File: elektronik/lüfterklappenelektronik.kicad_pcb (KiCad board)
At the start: 4 copper layers, 80 x 87.6 mm, 115 parts, among them J101 Conn_01x05_Male, J102 Ckmtw_2510S-2P, J103 Conn_LAN_ENC28J60, J104 USB_B_Micro, J106 WJ2EDGVC-5.08-2P, J107 WJ2EDGVC-5.08-2P, J108 WJ2EDGVC-5.08-2P, P101 PWR_BUS_CONN1, P103 PressureSensor3, P104 PressureSensor1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

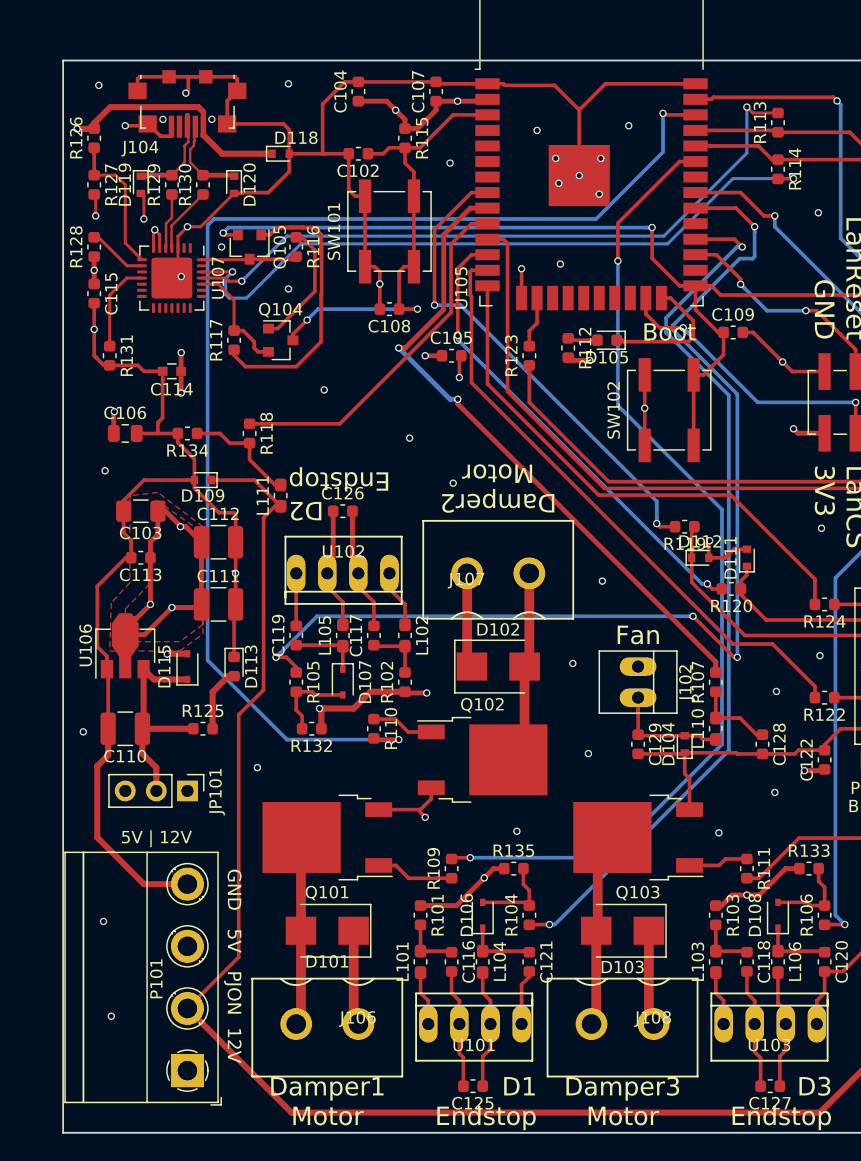
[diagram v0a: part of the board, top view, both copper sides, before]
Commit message: pcbnew: change footprint to vertical and fix fillzones and traces
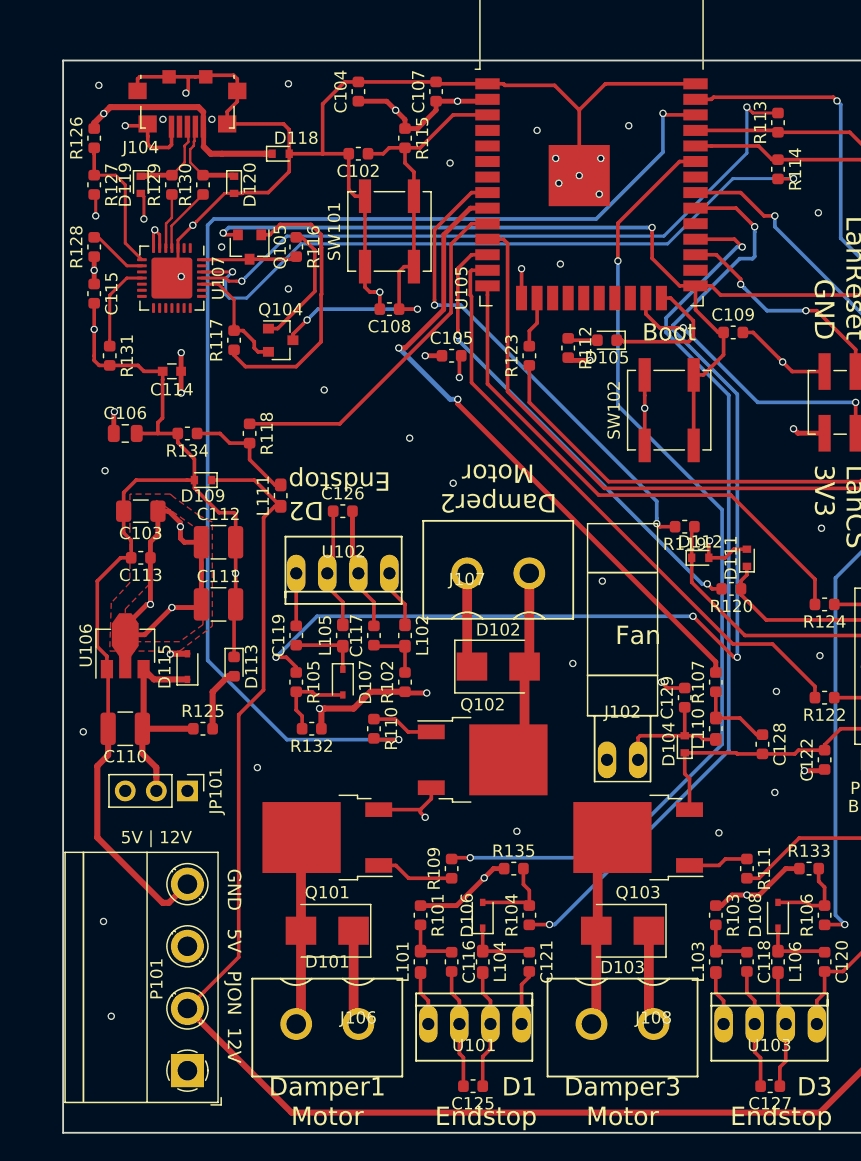
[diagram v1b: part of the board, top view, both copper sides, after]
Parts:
- C116: value 100P -> 100pF
- J102: footprint Connect:PINHEAD1-2 -> FootprintsTittelbach:C30436_pinhead_1x2_vertical_P2.54
- P101: value PWR_BUS_CONN1 -> PWR_BUS_CONN
- P109: value PWR_BUS_CONN2 -> PWR_BUS_CONN
- R125: value 2K -> 2K(5%)
- moved J102 8.03 mm to (106.7, 106.7), turned to 0 degrees
- moved C129 5.39 mm to (113.0, 101.6), turned to 90 degrees
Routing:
- net GND: track 616.5 -> 627.2 mm
- net +3V3: track 313.7 -> 304.2 mm
- net /VBUS: track 71.3 -> 68.4 mm
- net /UCD-: track 9.45 -> 7.16 mm
- net Net-(C129-Pad1): track 9.54 -> 10.7 mm

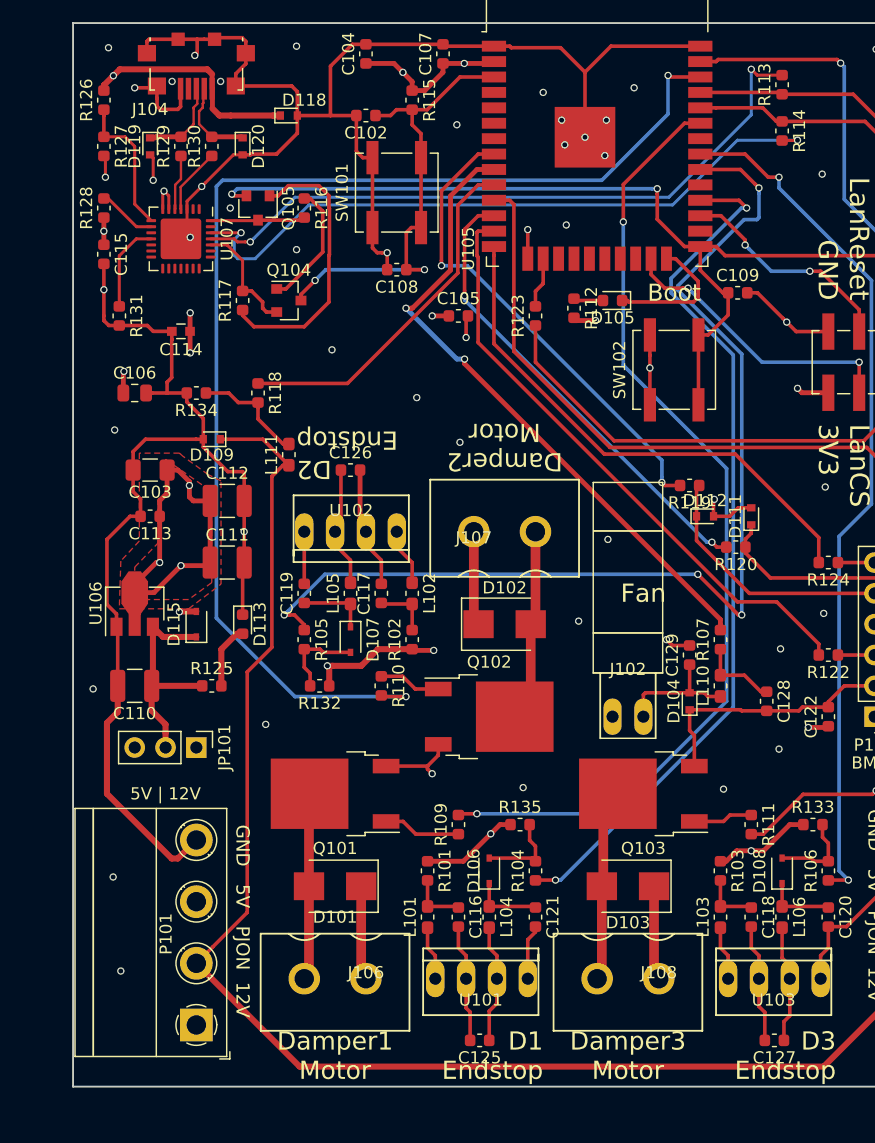
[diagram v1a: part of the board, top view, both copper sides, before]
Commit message: pcbnew: improve silk layer
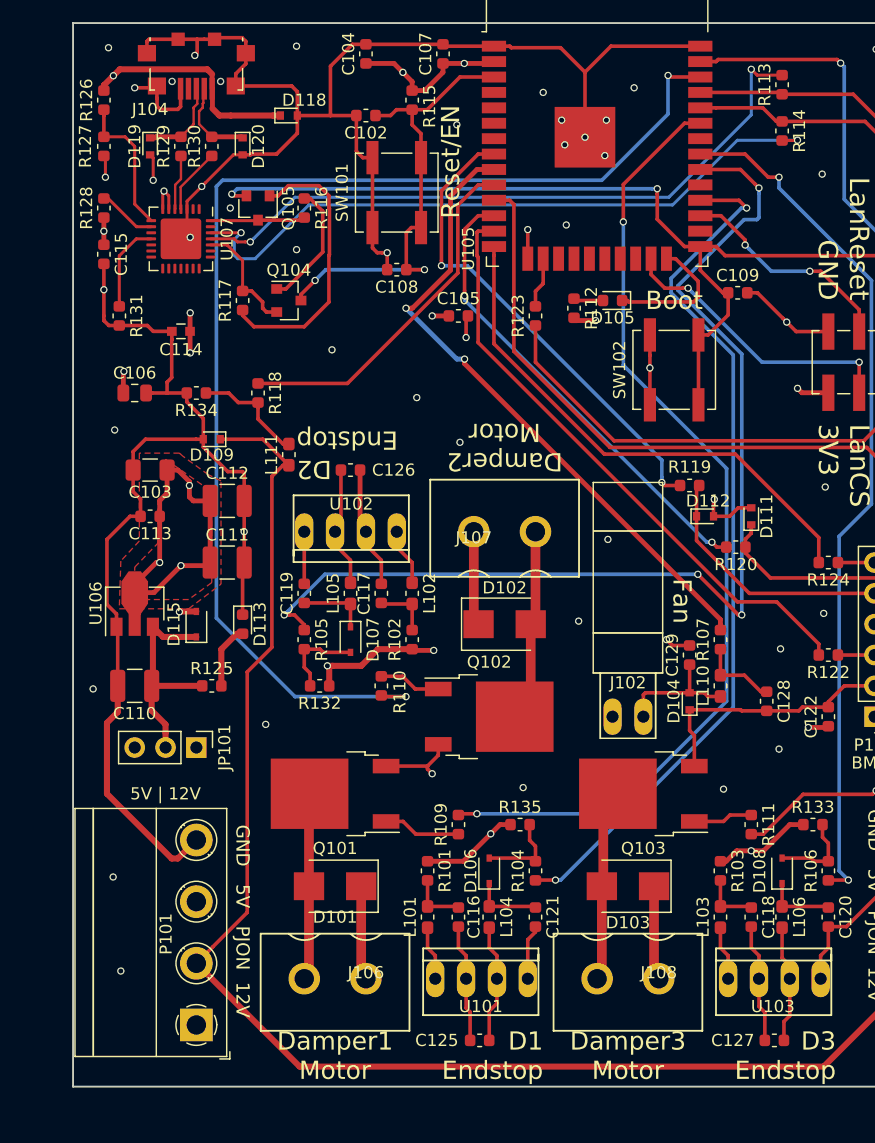
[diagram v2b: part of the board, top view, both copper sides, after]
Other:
- board text added: "Reset/EN"
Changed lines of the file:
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@@
   (general
     (thickness 1.6)
-    (drawings 34)
+    (drawings 35)
     (tracks 1040)
     (zones 0)
@@
   (module FootprintsTittelbach:C30436_pinhead_1x2_vertical_P2.54 (layer F.Cu)
     (at 106.68 106.68)
-    (fp_text reference J102 (at 1.27 -3.9) (layer F.SilkS)
+    (fp_text reference J102 (at 1.27 -2.794) (layer F.SilkS)
       (effects (font (size 1 1) (thickness 0.15)))
     )
@@
   (module FootprintsTittelbach:Ckmtw_2510S-4P (layer F.Cu)
     (at 116.205 128.27)
-    (fp_text reference U103 (at 3.75 1.75) (layer F.SilkS)
+    (fp_text reference U103 (at 3.683 2.286) (layer F.SilkS)
       (effects (font (size 1 1) (thickness 0.15)))
     )
@@
   (module FootprintsTittelbach:Ckmtw_2510S-4P (layer F.Cu)
     (at 88.9 91.44 180)
-    (fp_text reference U102 (at 3.75 1.75) (layer F.SilkS)
+    (fp_text reference U102 (at 3.75 2.286) (layer F.SilkS)
       (effects (font (size 1 1) (thickness 0.15)))
     )
@@
   (module FootprintsTittelbach:Ckmtw_2510S-4P (layer F.Cu)
     (at 92.075 128.27)
-    (fp_text reference U101 (at 3.75 1.75 180) (layer F.SilkS)
+    (fp_text reference U101 (at 3.75 2.286 180) (layer F.SilkS)
       (effects (font (size 1 1) (thickness 0.15)))
     )
@@
     (tags resistor)
     (attr smd)
-    (fp_text reference R110 (at 0 -1.43 90) (layer F.SilkS)
+    (fp_text reference R110 (at 0.508 -1.524 90) (layer F.SilkS)
       (effects (font (size 1 1) (thickness 0.15)))
     )
@@
     (tags SOD-323)
     (attr smd)
-    (fp_text reference D106 (at 0 -1.27 90) (layer F.SilkS)
+    (fp_text reference D106 (at 0 -1.524 90) (layer F.SilkS)
       (effects (font (size 1 1) (thickness 0.15)))
     )
@@
     (tags resistor)
     (attr smd)
-    (fp_text reference R127 (at 0 -1.43 90) (layer F.SilkS)
+    (fp_text reference R127 (at 0 1.524 90) (layer F.SilkS)
       (effects (font (size 1 1) (thickness 0.15)))
     )
@@
     (tags resistor)
     (attr smd)
-    (fp_text reference R119 (at 0 -1.43) (layer F.SilkS)
+    (fp_text reference R119 (at 0 1.524) (layer F.SilkS)
       (effects (font (size 1 1) (thickness 0.15)))
     )
@@
     (tags resistor)
     (attr smd)
-    (fp_text reference R115 (at 0 -1.43 90) (layer F.SilkS)
+    (fp_text reference R115 (at 0.508 -1.43 90) (layer F.SilkS)
       (effects (font (size 1 1) (thickness 0.15)))
     )
@@
     (tags "Diode SOD523")
     (attr smd)
-    (fp_text reference D112 (at 0 -1.3) (layer F.SilkS)
+    (fp_text reference D112 (at 0.254 -1.27) (layer F.SilkS)
       (effects (font (size 1 1) (thickness 0.15)))
     )
@@
     (tags "Diode SOD523")
     (attr smd)
-    (fp_text reference D111 (at 0 -1.3 90) (layer F.SilkS)
+    (fp_text reference D111 (at 0 1.27 90) (layer F.SilkS)
       (effects (font (size 1 1) (thickness 0.15)))
     )
@@
     (tags capacitor)
     (attr smd)
-    (fp_text reference C116 (at 0 -1.43 90) (layer F.SilkS)
+    (fp_text reference C116 (at 0 -1.27 90) (layer F.SilkS)
       (effects (font (size 1 1) (thickness 0.15)))
     )
@@
     (tags capacitor)
     (attr smd)
-    (fp_text reference C125 (at 0 -1.43) (layer F.SilkS)
+    (fp_text reference C125 (at 3.5305 0) (layer F.SilkS)
       (effects (font (size 1 1) (thickness 0.15)))
     )
@@
     (tags capacitor)
     (attr smd)
-    (fp_text reference C126 (at 0 -1.43) (layer F.SilkS)
+    (fp_text reference C126 (at 3.556 0) (layer F.SilkS)
       (effects (font (size 1 1) (thickness 0.15)))
     )
@@
     (tags capacitor)
     (attr smd)
-    (fp_text reference C127 (at 0 -1.43) (layer F.SilkS)
+    (fp_text reference C127 (at 3.429 0) (layer F.SilkS)
       (effects (font (size 1 1) (thickness 0.15)))
     )
@@
     )
   )
+  (gr_text Reset/EN (at 93.345 60.96 90) (layer F.SilkS)
+    (effects (font (size 1.5 1.5) (thickness 0.3)))
+  )
+  (gr_text Boot (at 111.76 72.39) (layer F.SilkS)
+    (effects (font (size 1.5 1.5) (thickness 0.3)))
+  )
   (dimension 87.63 (width 0.15) (layer Cmts.User)
     (gr_text "87,630 mm" (at 179.1 93.345 90) (layer Cmts.User)
@@
     (effects (font (size 1.4 1.4) (thickness 0.15)))
   )
-  (gr_text Boot (at 111.76 71.755) (layer F.SilkS)
-    (effects (font (size 1.4 1.4) (thickness 0.15)))
-  )
   (gr_text "5V | 12V" (at 69.85 113.03) (layer F.SilkS)
     (effects (font (size 1 1) (thickness 0.15)))
@@
     (effects (font (size 1 1) (thickness 0.15)))
   )
-  (gr_text Fan (at 109.22 96.52) (layer F.SilkS)
+  (gr_text Fan (at 112.395 97.155 270) (layer F.SilkS)
     (effects (font (size 1.5 1.5) (thickness 0.3)))
   )
